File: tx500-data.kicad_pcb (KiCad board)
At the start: 2 copper layers, 79 x 50 mm, 46 parts, among them J1 USB_B, J2 CAT, J3 REM/DATA, J4 USB_A, U1 TUSB2036, U2 FT232RL, U3 HS-100B, U4 TPS76333, Y1 6MHz

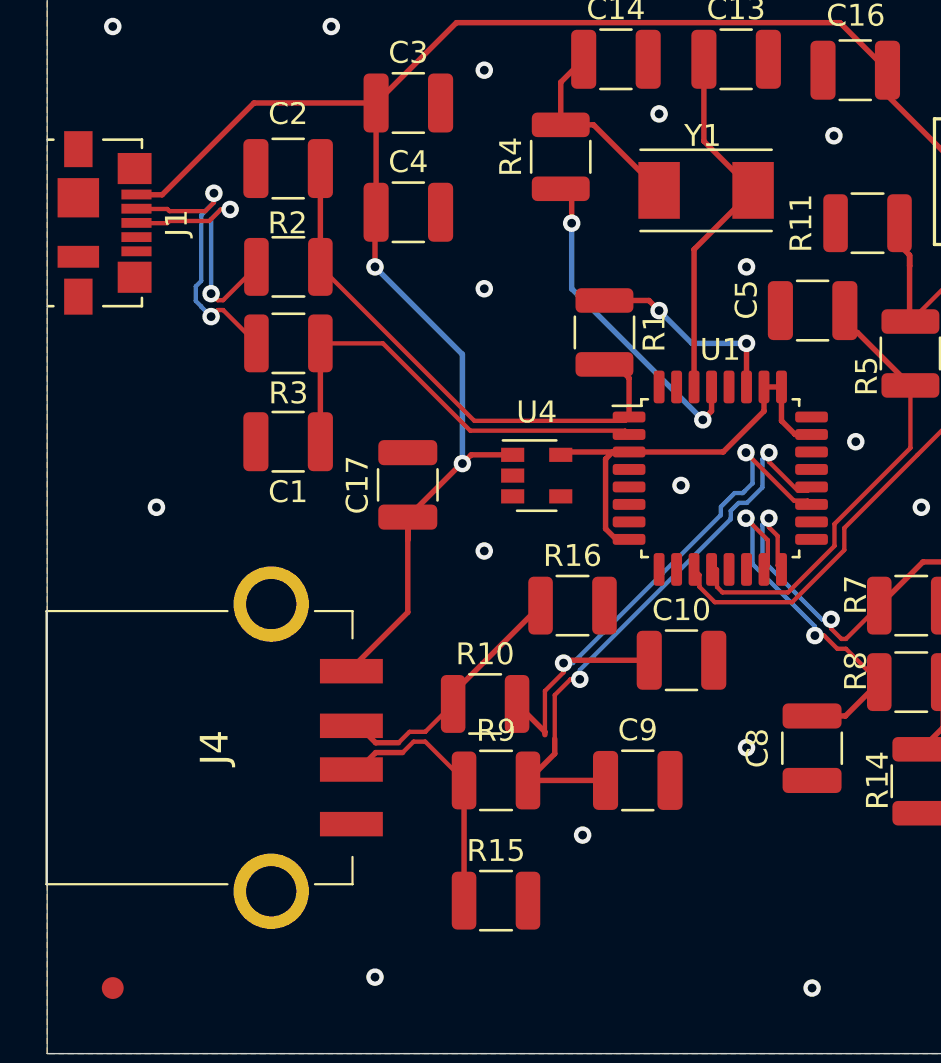
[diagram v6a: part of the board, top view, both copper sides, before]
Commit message: Adjust USB connectors to start case CAD
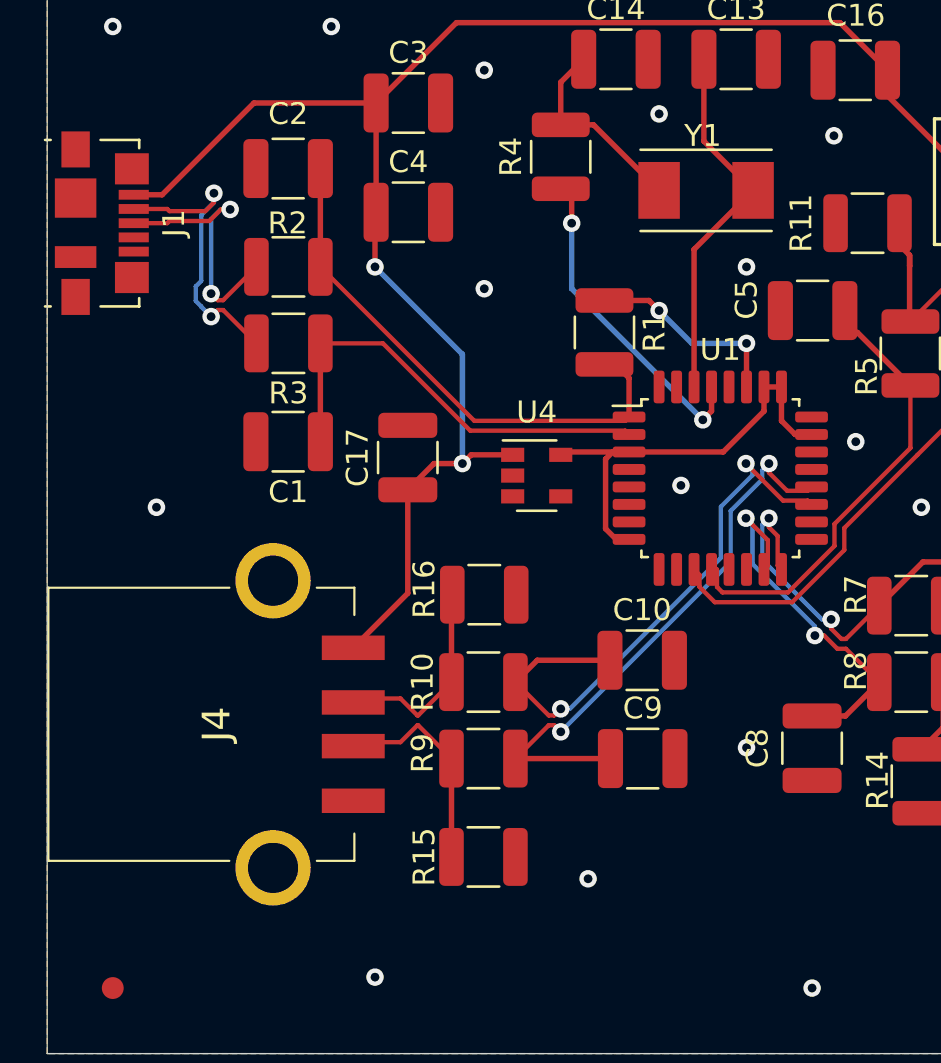
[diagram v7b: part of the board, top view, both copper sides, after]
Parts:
- J1: value USB_B -> USB_B_Micro
- moved R16 4.07 mm to (130.0, 99.0)
- moved R15 2.08 mm to (130.0, 111.0)
- moved C10 1.80 mm to (137.2, 102.0)
- moved C17 1.25 mm to (126.5, 92.7)
- moved R9 1.15 mm to (130.0, 106.5)
- moved J4 1.07 mm to (117.8, 104.9)
- moved C9 1.02 mm to (137.2, 106.5)
- moved R10 1.00 mm to (130.0, 103.0)
- moved J1 0.13 mm to (112.5, 82.0)
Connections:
- J1 pad 4: GNDREF -> (no net)
- J1 pad 5: (no net) -> GNDREF
- J1 pad 6: (no net) -> Net-(J1-Pad6)
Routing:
- net /Downstream USB/D-: track 11.5 -> 9.96 mm
- net /Downstream USB/D+: track 11.1 -> 9.95 mm
- net VBUS: track 119.1 -> 118.3 mm, vias 3 -> 2
- net /D3-: track 27.3 -> 26.6 mm

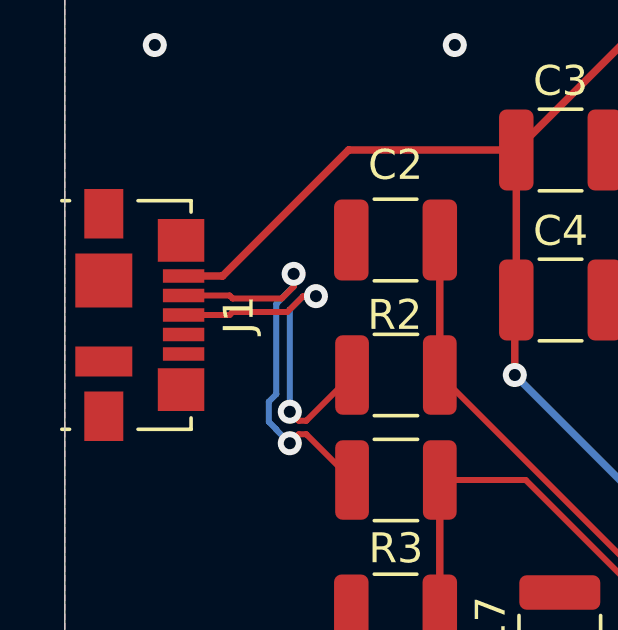
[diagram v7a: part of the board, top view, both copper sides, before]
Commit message: Reorganize onto one page
Suggested by eevblog.com/forum user teksturi, with thanks! https://www.eevblog.com/forum/oshw/advice-on-a-custom-usb-device/msg3518118/#msg3518118
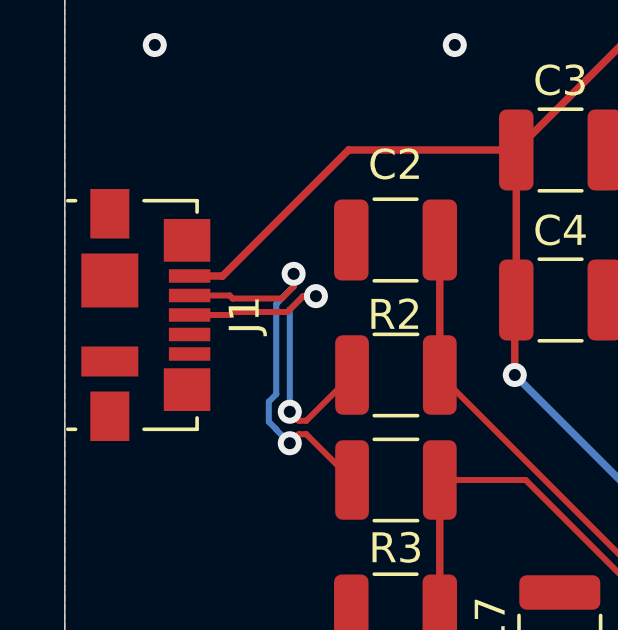
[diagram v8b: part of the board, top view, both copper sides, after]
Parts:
- moved J1 0.20 mm to (112.7, 82.0)
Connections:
- net /3V3 renamed +3V3
- net /Audio Interface/D+ renamed Net-(R13-Pad1)
- net /Audio Interface/D- renamed Net-(R14-Pad1)
- net /Audio Interface/LineOut renamed Net-(C12-Pad2)
- net /Audio Interface/MIC renamed /MIC
- net /Audio Interface/SPK renamed /SPK
- net /CAT Conrol/3V3 renamed /3V3IO
- net /CAT Conrol/D+ renamed Net-(R11-Pad1)
- net /CAT Conrol/D- renamed Net-(R12-Pad1)
- net /CAT Conrol/RXD renamed /RXD
- net /CAT Conrol/TXD renamed /TXD
- net /Downstream USB/D+ renamed Net-(J4-Pad3)
- net /Downstream USB/D- renamed Net-(J4-Pad2)
- net /Upstream USB/DR+ renamed /DR+
- net /Upstream USB/DR- renamed /DR-
- R4 pad 1: /XTAL2 -> Net-(C14-Pad1)
- R4 pad 2: Net-(C14-Pad1) -> /XTAL2
